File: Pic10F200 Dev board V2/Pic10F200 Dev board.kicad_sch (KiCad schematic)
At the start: 13 parts, among them J1 USB_C_Receptacle_PowerOnly_6P, J2 Conn_01x06_Pin, SW1 SW_Push, U1 PIC10F200-IOT

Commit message: Cleaned Schematic and PCB layout
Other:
- company: (none) -> Julien UHRY
- title: (none) -> PIC10F200 Dev Board
- moved on the sheet: C1, C2, C3, D1, D2, J1, J2, R1, R2, R3, R4, SW1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

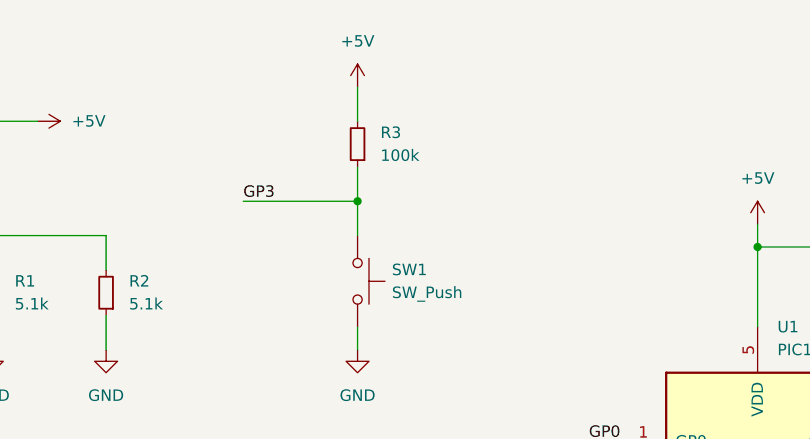
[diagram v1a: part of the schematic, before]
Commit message: Added different vibe coded examples as a demo for the dev board
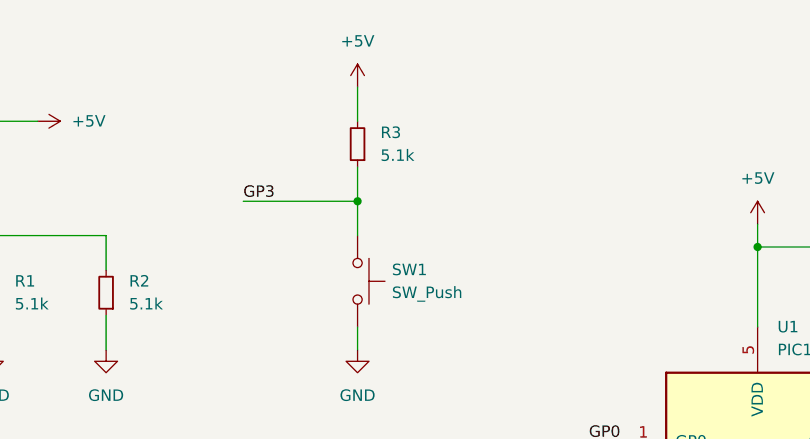
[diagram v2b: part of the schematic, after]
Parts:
- R3: value 100k -> 5.1k
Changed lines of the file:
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@@
 			)
 		)
-		(property "Value" "100k"
+		(property "Value" "5.1k"
 			(at 90.17 34.2899 0)
 			(show_name no)
